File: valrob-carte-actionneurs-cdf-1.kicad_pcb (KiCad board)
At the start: 4 copper layers, 125 parts, among them J1 USB_C_Receptacle_USB2.0_14P, J2 Conn_01x02, J3 Conn_01x02, J4 Conn_01x04_Pin, J5 Conn_01x02, J6 Conn_01x02, M1 Motor_Servo, M10 Motor_Servo, M11 Motor_Servo, M12 Motor_Servo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

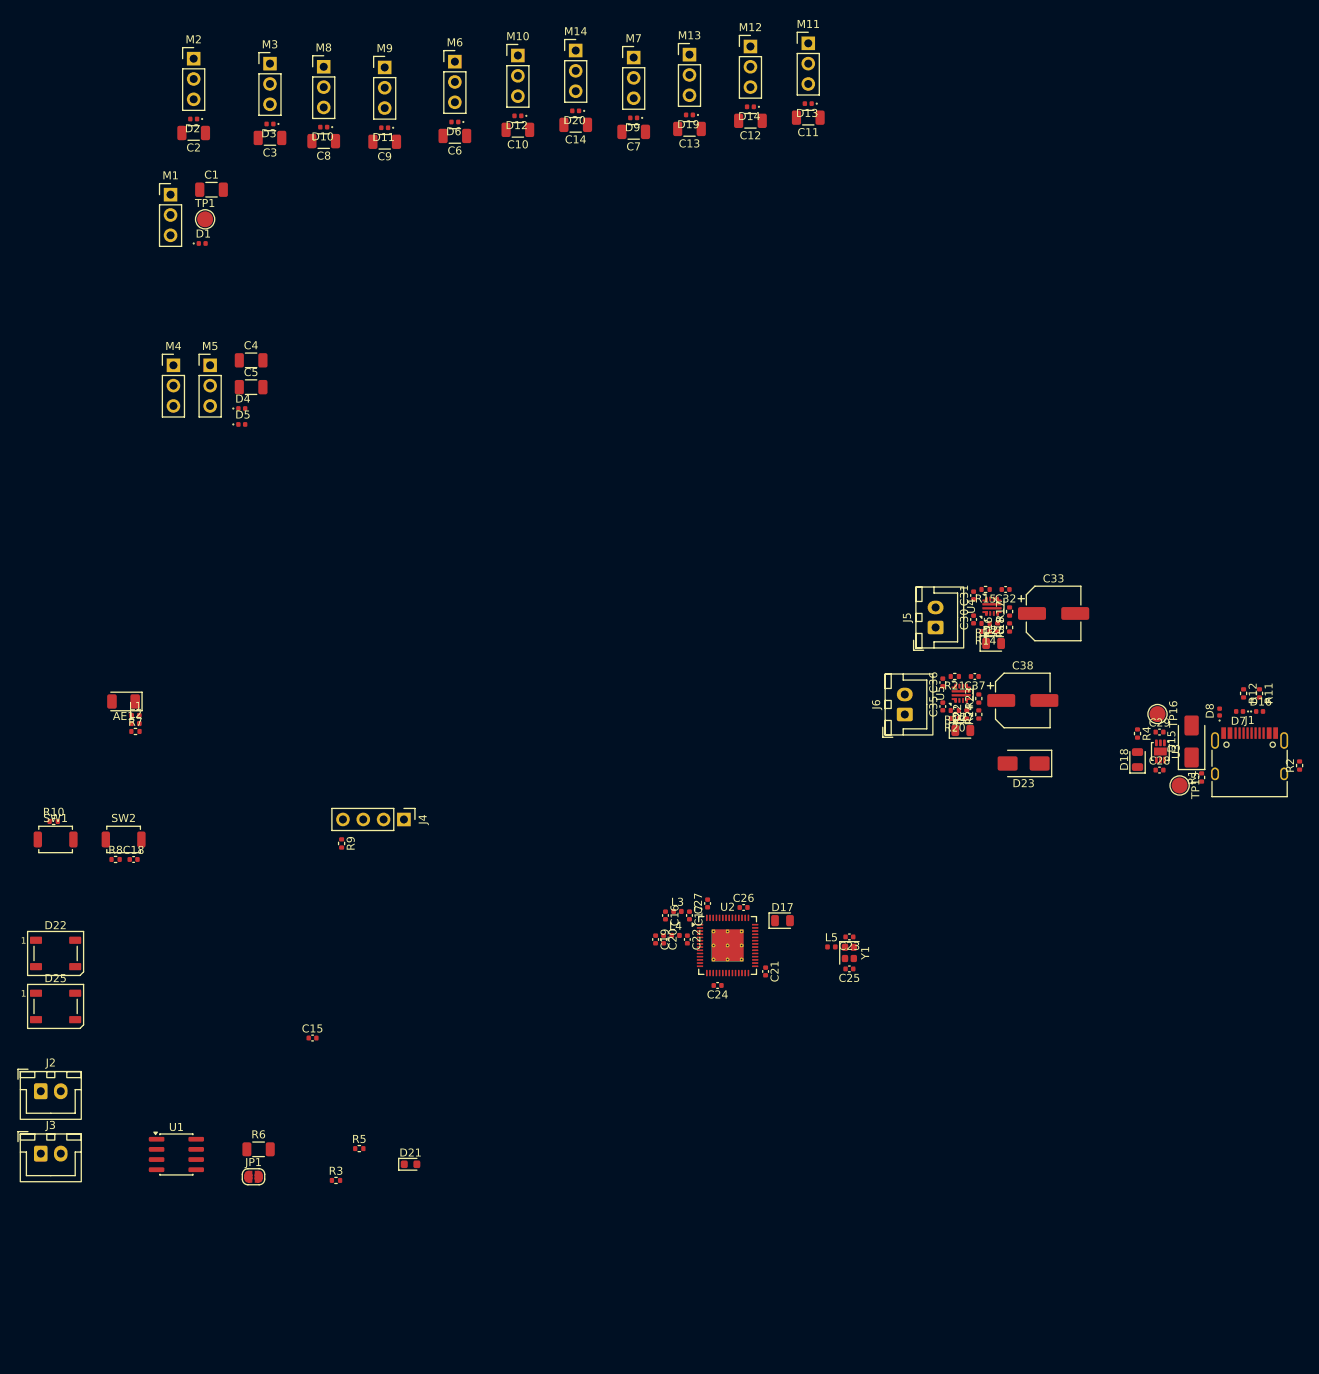
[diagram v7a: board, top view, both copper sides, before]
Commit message: pcb: add initial layout
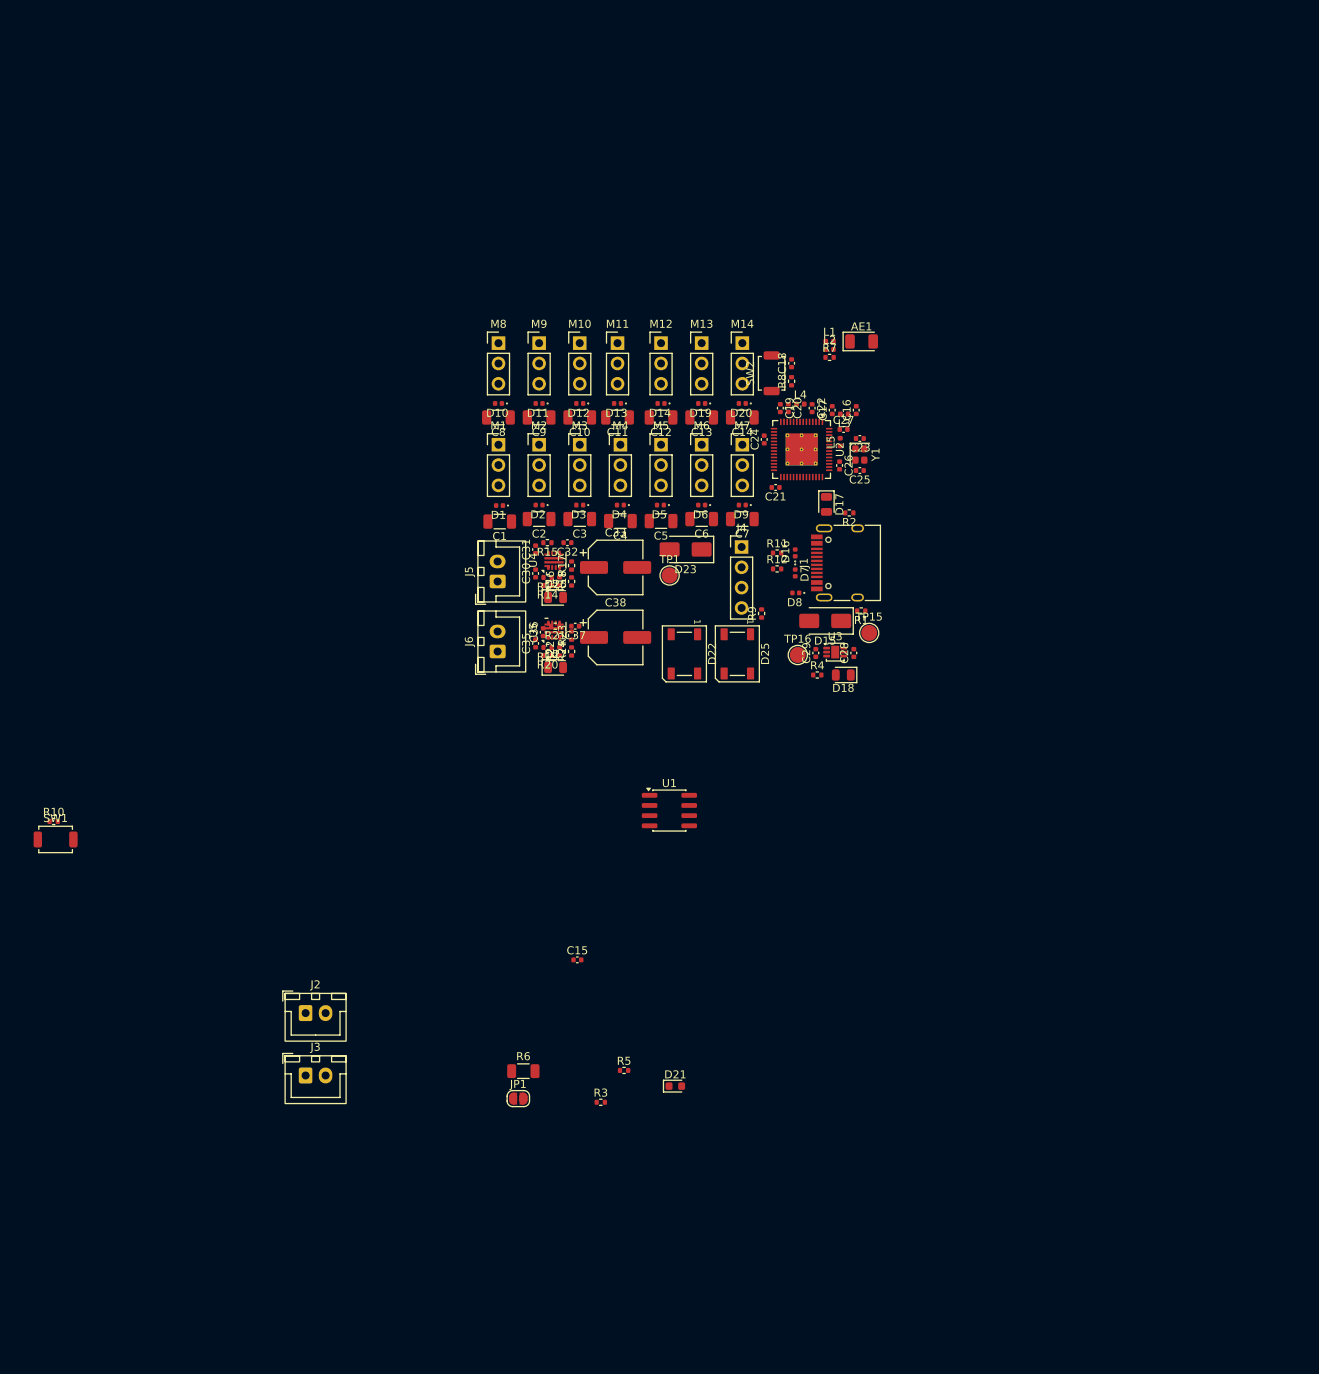
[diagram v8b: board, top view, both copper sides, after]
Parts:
- moved R8 103.5 mm to (123.0, 65.7), turned to 90 degrees
- moved C18 103.0 mm to (123.0, 63.5), turned to 90 degrees
- moved AE1 102.6 mm to (131.8, 60.8), turned to 0 degrees
- moved SW2 99.8 mm to (120.5, 64.7), turned to 90 degrees
- moved L1 98.6 mm to (127.8, 60.7)
- moved L2 98.6 mm to (127.8, 61.8)
- moved R7 98.6 mm to (127.8, 62.7)
- moved D25 95.9 mm to (116.2, 99.8), turned to -90 degrees
- moved D22 87.1 mm to (109.6, 99.8), turned to -90 degrees
- moved U1 75.1 mm to (107.7, 119.4)
- moved TP1 73.2 mm to (107.8, 90.0)
- moved C24 68.5 mm to (119.6, 73.0), turned to 90 degrees
- moved C19 68.2 mm to (121.6, 69.1)
- moved C20 68.2 mm to (122.6, 69.1)
- moved C22 68.2 mm to (125.6, 69.1)
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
